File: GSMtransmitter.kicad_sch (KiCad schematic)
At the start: 44 parts, among them J1 Conn_01x06_Pin, J2 Conn_02x02_2.54, J3 Conn_01x05, SW1 SM5-180UP-1, U1 STM32L052C8Tx, Y1 4 MHz, Y2 32768 kHz

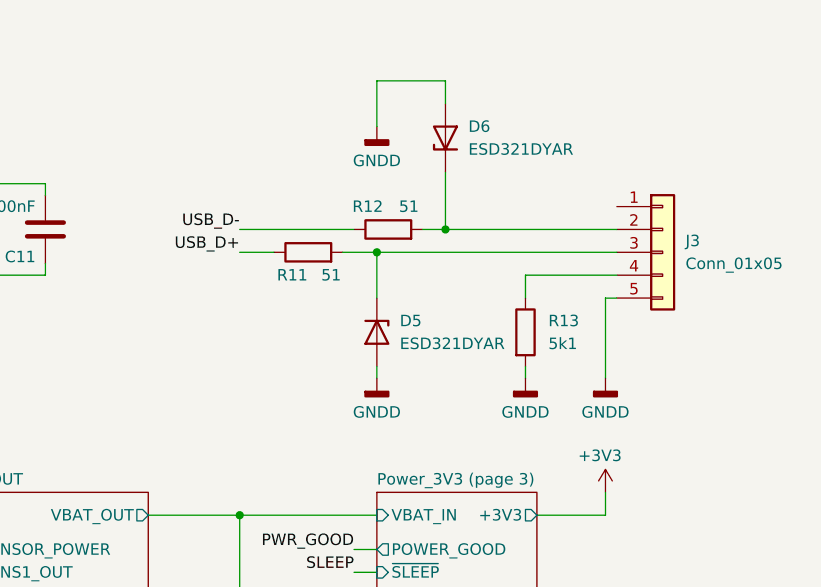
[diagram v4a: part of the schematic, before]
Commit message: USB pinout fixed
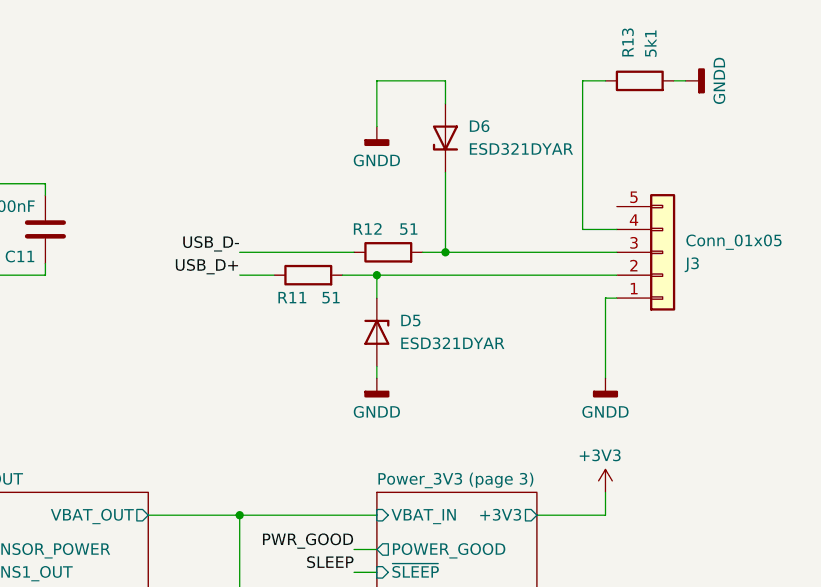
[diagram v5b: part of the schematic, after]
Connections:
- net GNDD: now also J3.1 (Pin_1); no longer J3.5 (Pin_5)
- net at D6.1 (K), R12.2: now also J3.3 (Pin_3); no longer J3.2 (Pin_2)
- net at D5.1 (K), R11.2: now also J3.2 (Pin_2); no longer J3.3 (Pin_3)
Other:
- moved on the sheet: R11, R12, R13
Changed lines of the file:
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@@
 	)
 	(junction
-		(at 243.84 38.1)
+		(at 243.84 40.64)
 		(diameter 0)
 		(color 0 0 0 0)
@@
 	)
 	(junction
-		(at 236.22 40.64)
-		(diameter 0)
-		(color 0 0 0 0)
-	)
-	(junction
 		(at 78.74 66.04)
 		(diameter 0)
@@
 	)
 	(junction
+		(at 236.22 43.18)
+		(diameter 0)
+		(color 0 0 0 0)
+	)
+	(junction
 		(at 190.5 33.02)
 		(diameter 0)
@@
 	(wire
 		(pts
-			(xy 220.98 38.1) (xy 233.68 38.1)
+			(xy 220.98 40.64) (xy 233.68 40.64)
 		)
 		(stroke
@@
 	(wire
 		(pts
+			(xy 243.84 40.64) (xy 262.89 40.64)
+		)
+		(stroke
+			(width 0)
+			(type default)
+		)
+	)
+	(wire
+		(pts
 			(xy 254 114.3) (xy 264.16 114.3)
 		)
@@
 	(wire
 		(pts
-			(xy 220.98 40.64) (xy 224.79 40.64)
+			(xy 220.98 43.18) (xy 224.79 43.18)
 		)
 		(stroke
@@
 	(wire
 		(pts
+			(xy 259.08 38.1) (xy 259.08 21.59)
+		)
+		(stroke
+			(width 0)
+			(type default)
+		)
+	)
+	(wire
+		(pts
 			(xy 144.78 76.2) (xy 147.32 76.2)
 		)
@@
 	(wire
 		(pts
-			(xy 236.22 45.72) (xy 236.22 40.64)
+			(xy 236.22 45.72) (xy 236.22 43.18)
 		)
 		(stroke
@@
 	(wire
 		(pts
-			(xy 252.73 45.72) (xy 252.73 43.18)
+			(xy 261.62 21.59) (xy 259.08 21.59)
 		)
 		(stroke
@@
 	(wire
 		(pts
-			(xy 236.22 40.64) (xy 262.89 40.64)
-		)
-		(stroke
-			(width 0)
-			(type default)
-		)
-	)
-	(wire
-		(pts
-			(xy 252.73 43.18) (xy 262.89 43.18)
-		)
-		(stroke
-			(width 0)
-			(type default)
-		)
-	)
-	(wire
-		(pts
 			(xy 36.83 53.34) (xy 39.37 53.34)
 		)
@@
 	(wire
 		(pts
-			(xy 232.41 40.64) (xy 236.22 40.64)
+			(xy 232.41 43.18) (xy 236.22 43.18)
 		)
 		(stroke
@@
 	(wire
 		(pts
-			(xy 92.71 129.54) (xy 109.22 129.54)
+			(xy 262.89 38.1) (xy 259.08 38.1)
 		)
 		(stroke
@@
 	(wire
 		(pts
-			(xy 262.89 45.72) (xy 261.62 45.72)
+			(xy 92.71 129.54) (xy 109.22 129.54)
 		)
 		(stroke
@@
 	(wire
 		(pts
+			(xy 236.22 43.18) (xy 262.89 43.18)
+		)
+		(stroke
+			(width 0)
+			(type default)
+		)
+	)
+	(wire
+		(pts
 			(xy 199.39 34.29) (xy 199.39 33.02)
 		)
@@
 	(wire
 		(pts
-			(xy 243.84 31.75) (xy 243.84 38.1)
+			(xy 243.84 31.75) (xy 243.84 40.64)
 		)
 		(stroke
@@
 	(wire
 		(pts
-			(xy 252.73 53.34) (xy 252.73 54.61)
+			(xy 269.24 21.59) (xy 270.51 21.59)
 		)
 		(stroke
@@
 	(wire
 		(pts
-			(xy 243.84 38.1) (xy 262.89 38.1)
+			(xy 261.62 45.72) (xy 262.89 45.72)
 		)
 		(stroke
@@
 	(wire
 		(pts
-			(xy 241.3 38.1) (xy 243.84 38.1)
+			(xy 241.3 40.64) (xy 243.84 40.64)
 		)
 		(stroke
@@
 	)
 	(label "USB_D+"
-		(at 220.98 40.64 180)
+		(at 220.98 43.18 180)
 		(effects
 			(font
@@
 	)
 	(label "USB_D-"
-		(at 220.98 38.1 180)
+		(at 220.98 40.64 180)
 		(effects
 			(font
@@
 	(symbol
 		(lib_id "power:GNDD")
-		(at 252.73 54.61 0)
+		(at 270.51 21.59 90)
 		(unit 1)
 		(exclude_from_sim no)
@@
 		(fields_autoplaced yes)
 		(property "Reference" "#PWR029"
-			(at 252.73 60.96 0)
+			(at 276.86 21.59 0)
 			(effects
 				(font
@@
 		)
 		(property "Value" "GNDD"
-			(at 252.73 58.42 0)
+			(at 274.32 21.59 0)
 			(effects
 				(font
@@
 		)
 		(property "Footprint" ""
-			(at 252.73 54.61 0)
+			(at 270.51 21.59 0)
 			(effects
 				(font
@@
 		)
 		(property "Datasheet" ""
-			(at 252.73 54.61 0)
+			(at 270.51 21.59 0)
 			(effects
 				(font
@@
 		)
 		(property "Description" "Power symbol creates a global label with name \"GNDD\" , digital ground"
-			(at 252.73 54.61 0)
+			(at 270.51 21.59 0)
 			(effects
 				(font
@@
 	(symbol
 		(lib_id "Device:R")
-		(at 237.49 38.1 90)
+		(at 237.49 40.64 90)
 		(unit 1)
 		(exclude_from_sim no)
@@
 		(dnp no)
 		(property "Reference" "R12"
-			(at 235.204 35.56 90)
+			(at 235.204 38.1 90)
 			(effects
 				(font
@@
 		)
 		(property "Value" "51"
-			(at 239.776 35.56 90)
+			(at 239.776 38.1 90)
 			(effects
 				(font
@@
 		)
 		(property "Footprint" "Resistor_SMD:R_0805_2012Metric_Pad1.20x1.40mm_HandSolder"
-			(at 237.49 39.878 90)
+			(at 237.49 42.418 90)
 			(effects
 				(font
@@
 		)
 		(property "Datasheet" "~"
-			(at 237.49 38.1 0)
+			(at 237.49 40.64 0)
 			(effects
 				(font
@@
 		)
 		(property "Description" "Resistor"
-			(at 237.49 38.1 0)
+			(at 237.49 40.64 0)
 			(effects
 				(font
@@
 	(symbol
 		(lib_id "Device:R")
-		(at 228.6 40.64 90)
+		(at 228.6 43.18 90)
 		(unit 1)
 		(exclude_from_sim no)
@@
 		(dnp no)
 		(property "Reference" "R11"
-			(at 226.822 43.18 90)
+			(at 226.822 45.72 90)
 			(effects
 				(font
@@
 		)
 		(property "Value" "51"
-			(at 231.14 43.18 90)
+			(at 231.14 45.72 90)
 			(effects
 				(font
@@
 		)
 		(property "Footprint" "Resistor_SMD:R_0805_2012Metric_Pad1.20x1.40mm_HandSolder"
-			(at 228.6 42.418 90)
+			(at 228.6 44.958 90)
 			(effects
 				(font
@@
 		)
 		(property "Datasheet" "~"
-			(at 228.6 40.64 0)
+			(at 228.6 43.18 0)
 			(effects
 				(font
@@
 		)
 		(property "Description" "Resistor"
-			(at 228.6 40.64 0)
+			(at 228.6 43.18 0)
 			(effects
 				(font
@@
 	(symbol
 		(lib_id "Device:R")
-		(at 252.73 49.53 0)
+		(at 265.43 21.59 90)
 		(unit 1)
 		(exclude_from_sim no)
@@
 		(fields_autoplaced yes)
 		(property "Reference" "R13"
-			(at 255.27 48.2599 0)
+			(at 264.1599 19.05 0)
 			(effects
 				(font
@@
 		)
 		(property "Value" "5k1"
-			(at 255.27 50.7999 0)
+			(at 266.6999 19.05 0)
 			(effects
 				(font
@@
 		)
 		(property "Footprint" "Resistor_SMD:R_0805_2012Metric_Pad1.20x1.40mm_HandSolder"
-			(at 250.952 49.53 90)
+			(at 265.43 23.368 90)
 			(effects
 				(font
@@
 		)
 		(property "Datasheet" "~"
-			(at 252.73 49.53 0)
+			(at 265.43 21.59 0)
 			(effects
 				(font
@@
 		)
 		(property "Description" "Resistor"
-			(at 252.73 49.53 0)
+			(at 265.43 21.59 0)
 			(effects
 				(font
@@
 		(lib_id "Connector_Generic:Conn_01x05")
 		(at 267.97 40.64 0)
+		(mirror x)
 		(unit 1)
 		(exclude_from_sim no)
@@
 		(on_board yes)
 		(dnp no)
-		(fields_autoplaced yes)
 		(property "Reference" "J3"
-			(at 270.51 39.3699 0)
+			(at 270.51 41.9101 0)
 			(effects
 				(font
@@
 		)
 		(property "Value" "Conn_01x05"
-			(at 270.51 41.9099 0)
+			(at 270.51 39.3701 0)
 			(effects
 				(font
